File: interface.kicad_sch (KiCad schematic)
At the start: 32 parts, among them J1 QTH-060-03-L-D-A, J2 WE_68715014522_ONE-SIDE, J3 WE_68715014022

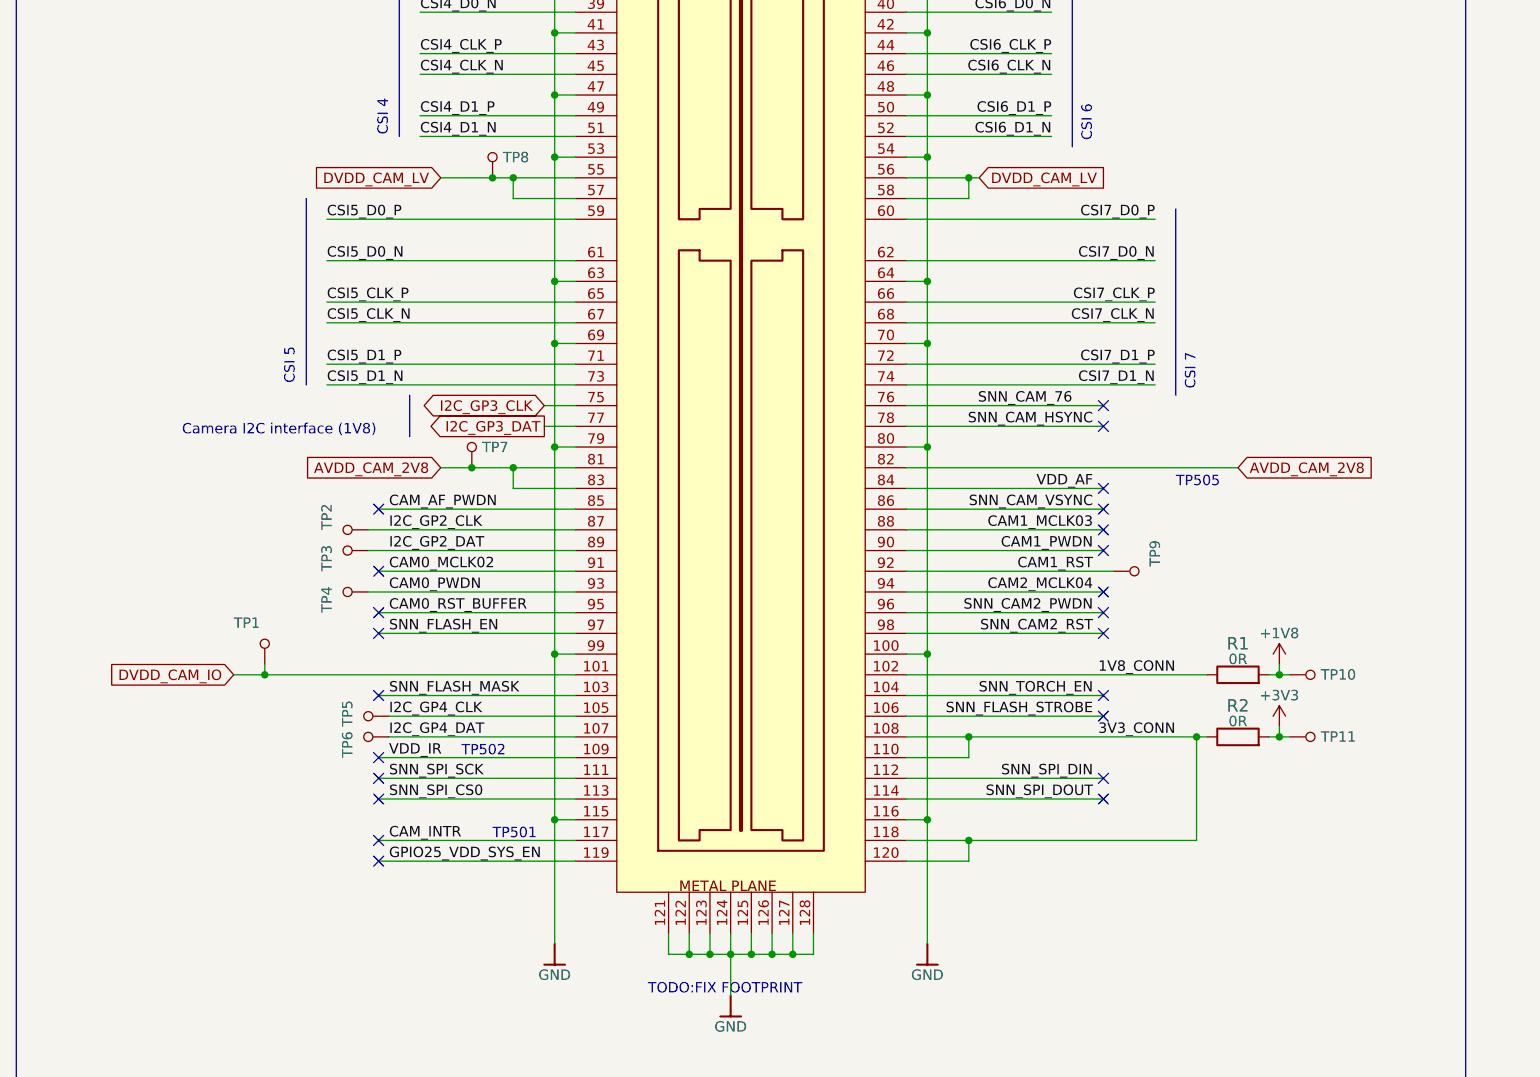
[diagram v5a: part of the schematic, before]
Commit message: Length matched CSI signals
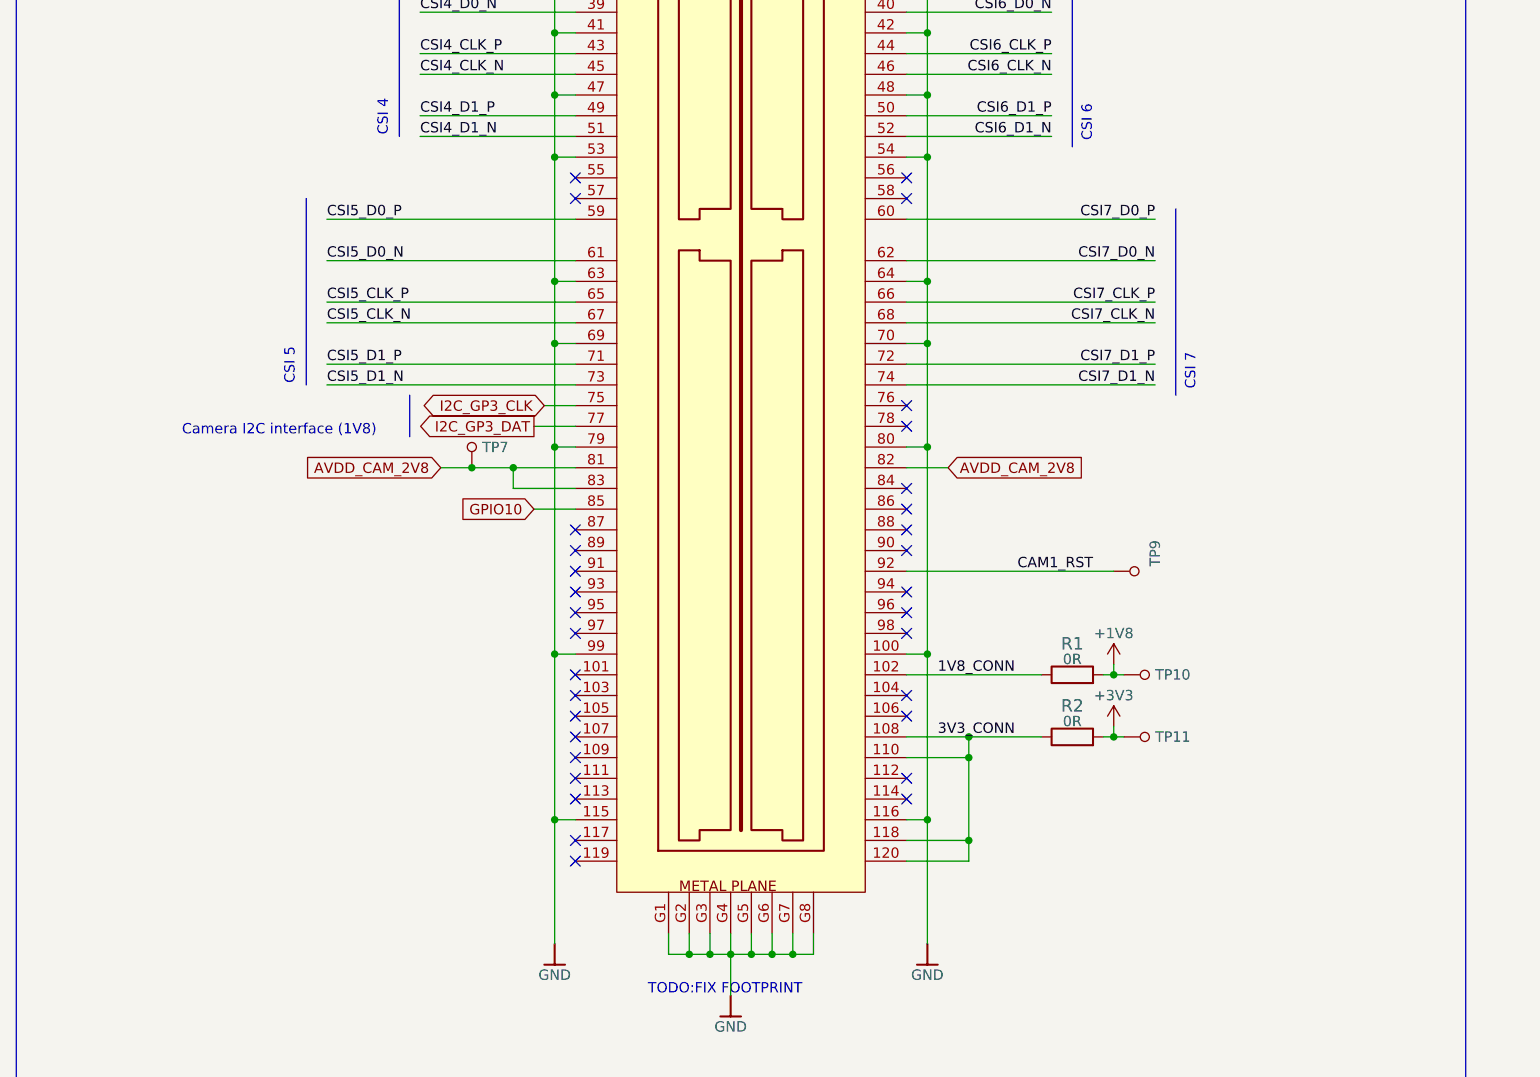
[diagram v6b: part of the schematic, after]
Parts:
- removed TP1, TP2, TP3, TP4, TP5, TP6, TP8: TP_SMD_0_75MM, antmicro-footprints:Testpoint_smd_0_75mm, symbol antmicroTestPoints:TP_SMD_0_75MM
- J1: Manufacturer (none) -> Samtec
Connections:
- net GND: now also J1.G1, J1.G2, J1.G3, J1.G4, J1.G5, J1.G6, J1.G7, J1.G8; no longer J1.121, J1.122, J1.123, J1.124, J1.125, J1.126, J1.127, J1.128
- net CAM0_MCLK02: no longer names the net of J1.91
- net CAM0_PWDN: no longer names the net of J1.93
- net CAM0_RST_BUFFER: no longer names the net of J1.95
- net CAM1_MCLK03: no longer names the net of J1.88
- net CAM1_PWDN: no longer names the net of J1.90
- net CAM2_MCLK04: no longer names the net of J1.94
- net CAM_AF_PWDN renamed GPIO10
- net CAM_INTR: no longer names the net of J1.117
- net DVDD_CAM_IO: no longer names the net of J1.101
- removed net DVDD_CAM_LV: J1.55, J1.56, J1.57, J1.58
- net GPIO25_VDD_SYS_EN: no longer names the net of J1.119
- net I2C_GP2_CLK: no longer names the net of J1.87
- net I2C_GP2_DAT: no longer names the net of J1.89
- net I2C_GP4_CLK: no longer names the net of J1.105
- net I2C_GP4_DAT: no longer names the net of J1.107
- net SNN_CAM2_PWDN: no longer names the net of J1.96
- net SNN_CAM2_RST: no longer names the net of J1.98
- net SNN_CAM_76: no longer names the net of J1.76
- net SNN_CAM_HSYNC: no longer names the net of J1.78
- net SNN_CAM_VSYNC: no longer names the net of J1.86
- net SNN_FLASH_EN: no longer names the net of J1.97
- net SNN_FLASH_MASK: no longer names the net of J1.103
- net SNN_FLASH_STROBE: no longer names the net of J1.106
- net SNN_SPI_CS0: no longer names the net of J1.113
- net SNN_SPI_DIN: no longer names the net of J1.112
- net SNN_SPI_DOUT: no longer names the net of J1.114
- net SNN_SPI_SCK: no longer names the net of J1.111
- net SNN_TORCH_EN: no longer names the net of J1.104
- net VDD_AF: no longer names the net of J1.84
- net VDD_IR: no longer names the net of J1.109
- no-connect marks 51 -> 60
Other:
- note removed: "TP501"
- note removed: "TP502"
- note removed: "TP505"
- moved on the sheet: R1, R2, TP10, TP11

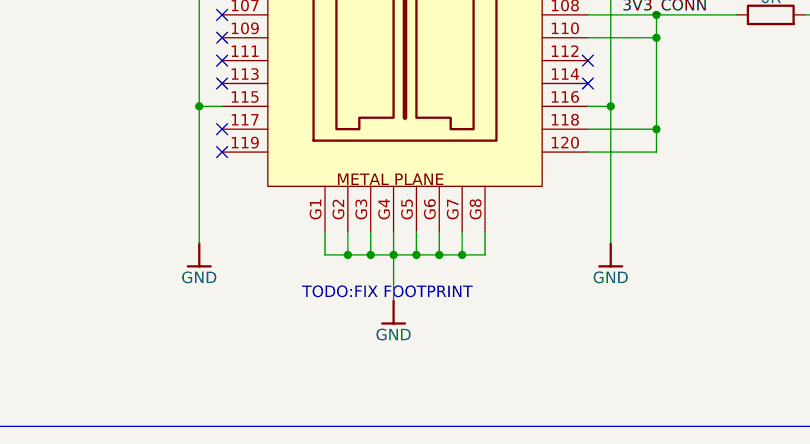
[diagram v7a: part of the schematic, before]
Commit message: Added loclib, updated README and added pdf schematic
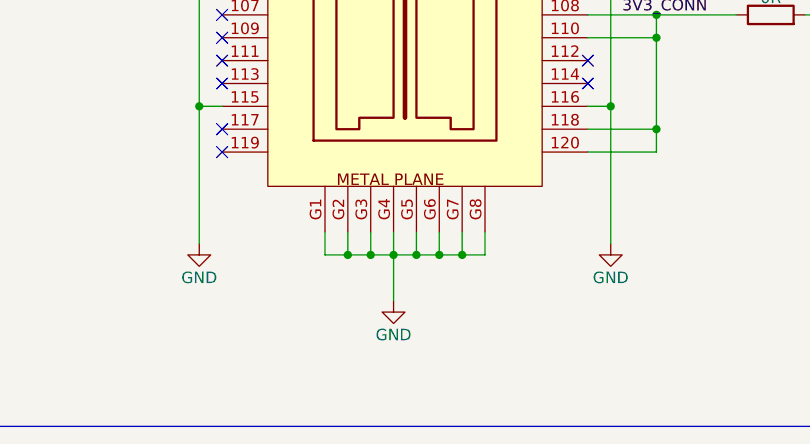
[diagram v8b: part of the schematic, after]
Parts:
- C1, C2, C3, C4: footprint antmicro-footprints:0603-cap -> antmicro-jetson-agx-csi-adapter-footprints:0603-cap; symbol antmicroCapacitors0603:C_1u_0603 -> antmicro-jetson-agx-csi-adapter:C_1u_0603
- D1, D2, D3, D4: footprint antmicro-footprints:LED_0603 -> antmicro-jetson-agx-csi-adapter-footprints:LED_0603; symbol antmicroLEDIndicationDiscrete:LTST-C190GKT -> antmicro-jetson-agx-csi-adapter:LTST-C190GKT
- F1, F2, F3, F4: footprint antmicro-footprints:0603-Fuse-Littelfuse-0467 -> antmicro-jetson-agx-csi-adapter-footprints:0603-Fuse-Littelfuse-0467; symbol antmicroFuses:04671.25NR -> antmicro-jetson-agx-csi-adapter:04671.25NR
- J1: footprint antmicro-footprints:SAMTEC_QTH-060-03-X-D-A -> antmicro-jetson-agx-csi-adapter-footprints:SAMTEC_QTH-060-03-X-D-A; symbol antmicroB2bConnectors:QTH-060-03-L-D-A -> antmicro-jetson-agx-csi-adapter:QTH-060-03-L-D-A
- J2: footprint antmicro-footprints:WE_68715014522_ONE-SIDE -> antmicro-jetson-agx-csi-adapter-footprints:WE_68715014522_ONE-SIDE; symbol antmicroFCCConnectors:WE_68715014522_ONE-SIDE -> antmicro-jetson-agx-csi-adapter:WE_68715014522_ONE-SIDE
- J3: footprint antmicro-footprints:WE_68715014022 -> antmicro-jetson-agx-csi-adapter-footprints:WE_68715014022; symbol antmicroFCCConnectors:WE_68715014022 -> antmicro-jetson-agx-csi-adapter:WE_68715014022
- R1, R2: footprint antmicro-footprints:0805-res -> antmicro-jetson-agx-csi-adapter-footprints:0805-res; symbol antmicroResistorsmisc:R_0R_0805 -> antmicro-jetson-agx-csi-adapter:R_0R_0805
- R3, R5: footprint antmicro-footprints:0402-res -> antmicro-jetson-agx-csi-adapter-footprints:0402-res; symbol antmicroResistors0402:R_200R_0402 -> antmicro-jetson-agx-csi-adapter:R_200R_0402
- R4, R6: footprint antmicro-footprints:0402-res -> antmicro-jetson-agx-csi-adapter-footprints:0402-res; symbol antmicroResistors0402:R_470R_0402 -> antmicro-jetson-agx-csi-adapter:R_470R_0402
- TP10, TP11, TP7, TP9: footprint antmicro-footprints:Testpoint_smd_0_75mm -> antmicro-jetson-agx-csi-adapter-footprints:Testpoint_smd_0_75mm; symbol antmicroTestPoints:TP_SMD_0_75MM -> antmicro-jetson-agx-csi-adapter:TP_SMD_0_75MM
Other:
- note removed: "TODO:FIX FOOTPRINT"
